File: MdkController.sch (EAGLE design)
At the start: 25 parts, among them M1 SILENTSTEPSTICK, M2 SILENTSTEPSTICK, M3 SILENTSTEPSTICK, M4 SILENTSTEPSTICK, M5 NRF8001-BREAKOUT, U1 ACPL-227, X1 1501_04, X2 1501_04, X3 1501_04

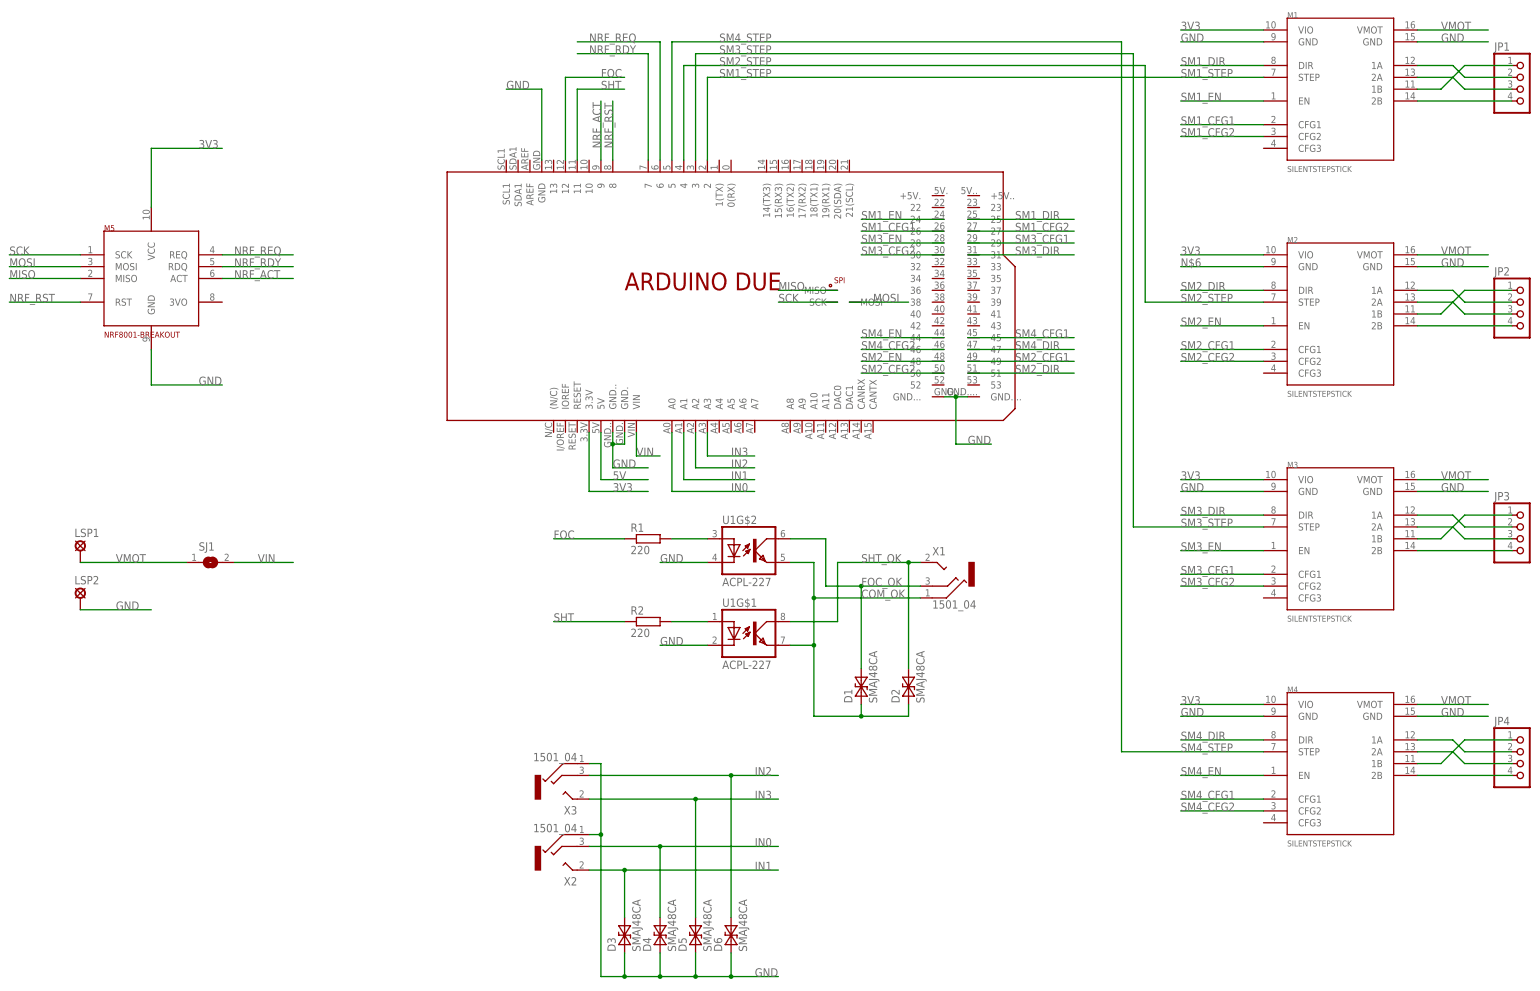
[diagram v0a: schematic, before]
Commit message: Überarbeitung (4. Stepper entfernt, etwas aufgeräumt)
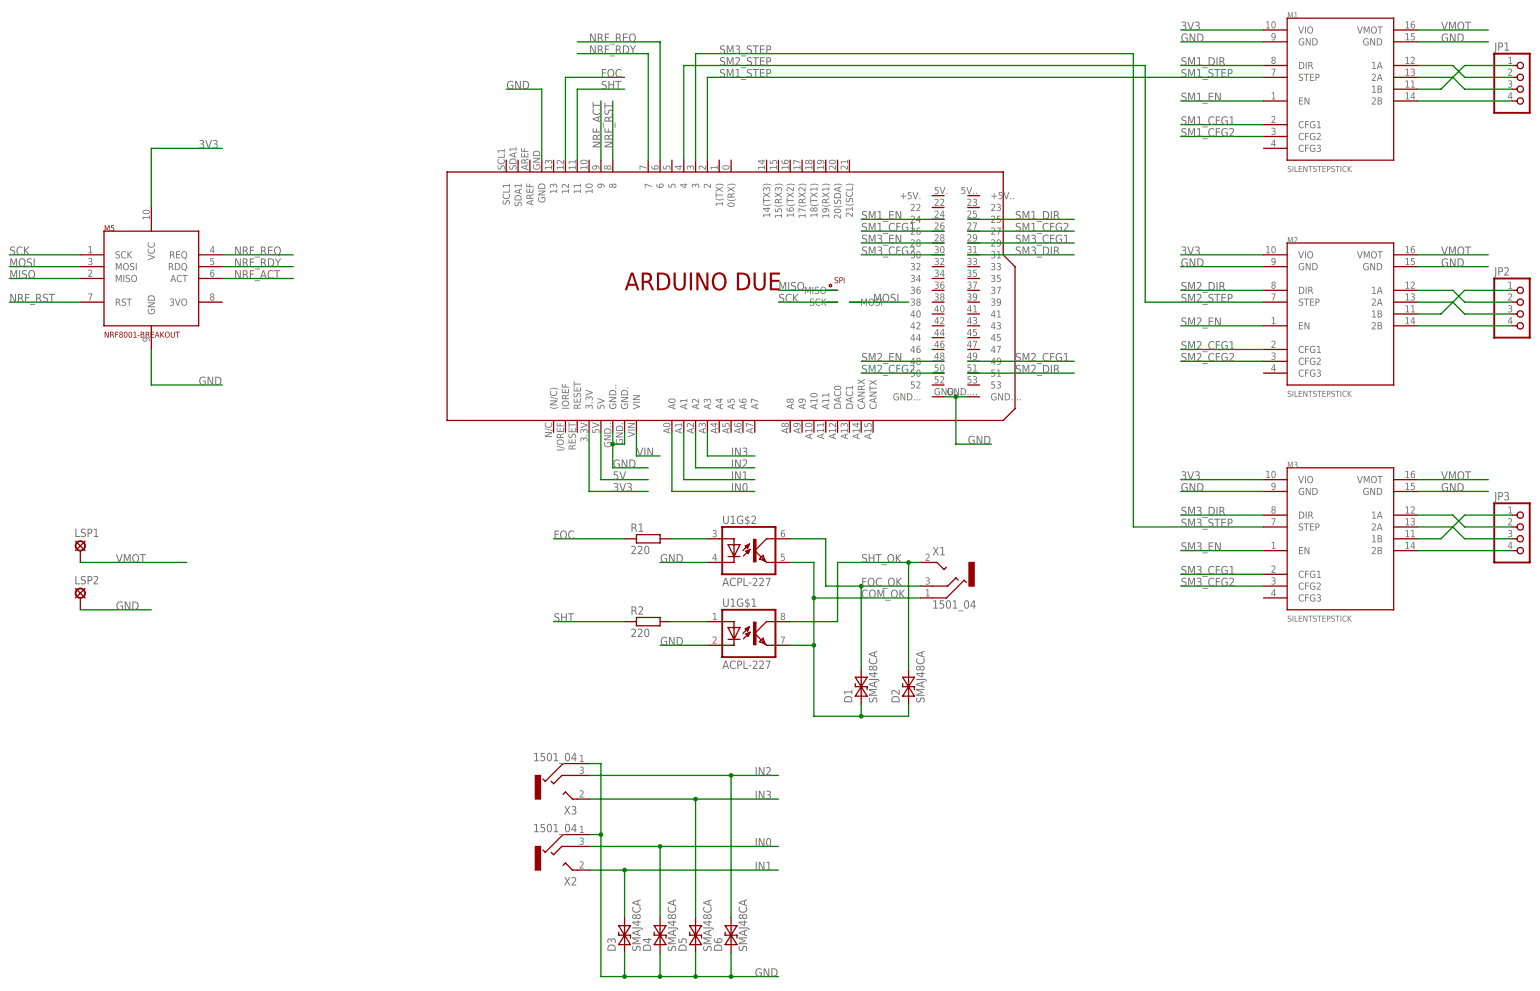
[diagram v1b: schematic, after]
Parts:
- removed JP4: (no value), pinhead:PINHD-1X4
- removed M4: SILENTSTEPSTICK, watterott:SILENTSTEPSTICK
- removed SJ1: (no value), jumper:SJ
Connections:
- removed net N$20: JP4.1, M4.1B
- removed net N$21: JP4.2, M4.1A
- removed net N$22: JP4.3, M4.2A
- removed net N$23: JP4.4, M4.2B
- removed net N$6: M2.GND@1
- removed net SM4_CFG1: M4.CFG1, U$1.45
- removed net SM4_CFG2: M4.CFG2, U$1.46
- removed net SM4_DIR: M4.DIR, U$1.47
- removed net SM4_EN: M4.EN, U$1.44
- removed net SM4_STEP: M4.STEP, U$1.5
- net 3V3: no longer M4.VIO
- net GND: now also M2.GND@1; no longer M4.GND@1, M4.GND@2
- net VIN: no longer SJ1.2
- net VMOT: no longer M4.VMOT, SJ1.1
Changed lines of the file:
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@@
 <?xml version="1.0" encoding="utf-8"?>
 <!DOCTYPE eagle SYSTEM "eagle.dtd">
-<eagle version="7.2.0">
+<eagle version="7.3.0">
 <drawing>
 <settings>
@@
 <part name="M2" library="watterott" deviceset="SILENTSTEPSTICK" device=""/>
 <part name="M3" library="watterott" deviceset="SILENTSTEPSTICK" device=""/>
-<part name="M4" library="watterott" deviceset="SILENTSTEPSTICK" device=""/>
 <part name="R1" library="rcl" deviceset="R-EU_" device="R0805" value="220"/>
 <part name="R2" library="rcl" deviceset="R-EU_" device="R0805" value="220"/>
@@
 <part name="JP2" library="pinhead" deviceset="PINHD-1X4" device=""/>
 <part name="JP3" library="pinhead" deviceset="PINHD-1X4" device=""/>
-<part name="JP4" library="pinhead" deviceset="PINHD-1X4" device=""/>
 <part name="LSP1" library="solpad" deviceset="SE14" device=""/>
 <part name="LSP2" library="solpad" deviceset="SE14" device=""/>
-<part name="SJ1" library="jumper" deviceset="SJ" device=""/>
 </parts>
 <sheets>
@@
 <instance part="M2" gate="G$1" x="215.9" y="134.62"/>
 <instance part="M3" gate="G$1" x="215.9" y="86.36"/>
-<instance part="M4" gate="G$1" x="215.9" y="38.1"/>
 <instance part="R1" gate="G$1" x="78.74" y="114.3"/>
 <instance part="R2" gate="G$1" x="78.74" y="96.52"/>
@@
 <instance part="JP2" gate="A" x="266.7" y="162.56"/>
 <instance part="JP3" gate="A" x="266.7" y="114.3"/>
-<instance part="JP4" gate="A" x="266.7" y="66.04"/>
 <instance part="LSP1" gate="1" x="-43.18" y="111.76"/>
 <instance part="LSP2" gate="1" x="-43.18" y="101.6"/>
-<instance part="SJ1" gate="1" x="-15.24" y="109.22"/>
 </instances>
 <busses>
@@
 </segment>
 </net>
-<net name="SM4_EN" class="0">
-<segment>
-<wire x1="142.24" y1="157.48" x2="124.46" y2="157.48" width="0.1524" layer="91"/>
-<pinref part="U$1" gate="G$1" pin="44"/>
-<label x="124.46" y="157.48" size="1.778" layer="95"/>
-</segment>
-<segment>
-<pinref part="M4" gate="G$1" pin="EN"/>
-<wire x1="210.82" y1="63.5" x2="193.04" y2="63.5" width="0.1524" layer="91"/>
-<label x="193.04" y="63.5" size="1.778" layer="95"/>
-</segment>
-</net>
-<net name="SM4_CFG1" class="0">
-<segment>
-<wire x1="147.32" y1="157.48" x2="170.18" y2="157.48" width="0.1524" layer="91"/>
-<pinref part="U$1" gate="G$1" pin="45"/>
-<label x="157.48" y="157.48" size="1.778" layer="95"/>
-</segment>
-<segment>
-<pinref part="M4" gate="G$1" pin="CFG1"/>
-<wire x1="210.82" y1="58.42" x2="193.04" y2="58.42" width="0.1524" layer="91"/>
-<label x="193.04" y="58.42" size="1.778" layer="95"/>
-</segment>
-</net>
 <net name="SM3_CFG2" class="0">
 <segment>
@@
 <wire x1="210.82" y1="104.14" x2="193.04" y2="104.14" width="0.1524" layer="91"/>
 <label x="193.04" y="104.14" size="1.778" layer="95"/>
-</segment>
-</net>
-<net name="SM4_DIR" class="0">
-<segment>
-<wire x1="147.32" y1="154.94" x2="170.18" y2="154.94" width="0.1524" layer="91"/>
-<pinref part="U$1" gate="G$1" pin="47"/>
-<label x="157.48" y="154.94" size="1.778" layer="95"/>
-</segment>
-<segment>
-<pinref part="M4" gate="G$1" pin="DIR"/>
-<wire x1="210.82" y1="71.12" x2="193.04" y2="71.12" width="0.1524" layer="91"/>
-<label x="193.04" y="71.12" size="1.778" layer="95"/>
-</segment>
-</net>
-<net name="SM4_CFG2" class="0">
-<segment>
-<wire x1="142.24" y1="154.94" x2="124.46" y2="154.94" width="0.1524" layer="91"/>
-<pinref part="U$1" gate="G$1" pin="46"/>
-<label x="124.46" y="154.94" size="1.778" layer="95"/>
-</segment>
-<segment>
-<pinref part="M4" gate="G$1" pin="CFG2"/>
-<wire x1="210.82" y1="55.88" x2="193.04" y2="55.88" width="0.1524" layer="91"/>
-<label x="193.04" y="55.88" size="1.778" layer="95"/>
 </segment>
 </net>
@@
 </segment>
 </net>
-<net name="SM4_STEP" class="0">
-<segment>
-<pinref part="U$1" gate="G$1" pin="5"/>
-<wire x1="83.82" y1="195.58" x2="83.82" y2="220.98" width="0.1524" layer="91"/>
-<wire x1="83.82" y1="220.98" x2="180.34" y2="220.98" width="0.1524" layer="91"/>
-<pinref part="M4" gate="G$1" pin="STEP"/>
-<wire x1="180.34" y1="220.98" x2="180.34" y2="68.58" width="0.1524" layer="91"/>
-<wire x1="180.34" y1="68.58" x2="210.82" y2="68.58" width="0.1524" layer="91"/>
-<label x="93.98" y="220.98" size="1.778" layer="95"/>
-<label x="193.04" y="68.58" size="1.778" layer="95"/>
-</segment>
-</net>
 <net name="3V3" class="1">
 <segment>
@@
 <wire x1="66.04" y1="124.46" x2="78.74" y2="124.46" width="0.1524" layer="91"/>
 <label x="71.12" y="124.46" size="1.778" layer="95"/>
-</segment>
-<segment>
-<pinref part="M4" gate="G$1" pin="VIO"/>
-<wire x1="210.82" y1="78.74" x2="193.04" y2="78.74" width="0.1524" layer="91"/>
-<label x="193.04" y="78.74" size="1.778" layer="95"/>
 </segment>
 <segment>
@@
 </segment>
 <segment>
-<pinref part="M4" gate="G$1" pin="GND@2"/>
-<wire x1="243.84" y1="76.2" x2="259.08" y2="76.2" width="0.1524" layer="91"/>
-<label x="248.92" y="76.2" size="1.778" layer="95"/>
-</segment>
-<segment>
-<pinref part="M4" gate="G$1" pin="GND@1"/>
-<wire x1="210.82" y1="76.2" x2="193.04" y2="76.2" width="0.1524" layer="91"/>
-<label x="193.04" y="76.2" size="1.778" layer="95"/>
-</segment>
-<segment>
 <pinref part="M3" gate="G$1" pin="GND@1"/>
 <wire x1="210.82" y1="124.46" x2="193.04" y2="124.46" width="0.1524" layer="91"/>
@@
 <wire x1="-43.18" y1="99.06" x2="-27.94" y2="99.06" width="0.1524" layer="91"/>
 <label x="-35.56" y="99.06" size="1.778" layer="95"/>
+</segment>
+<segment>
+<pinref part="M2" gate="G$1" pin="GND@1"/>
+<wire x1="210.82" y1="172.72" x2="193.04" y2="172.72" width="0.1524" layer="91"/>
+<label x="193.04" y="172.72" size="1.778" layer="95"/>
 </segment>
 </net>
@@
 </segment>
 </net>
-<net name="N$6" class="0">
-<segment>
-<pinref part="M2" gate="G$1" pin="GND@1"/>
-<wire x1="210.82" y1="172.72" x2="193.04" y2="172.72" width="0.1524" layer="91"/>
-<label x="193.04" y="172.72" size="1.778" layer="95"/>
-</segment>
-</net>
 <net name="N$3" class="2">
 <segment>
@@
 </segment>
 </net>
-<net name="N$20" class="2">
-<segment>
-<pinref part="M4" gate="G$1" pin="1B"/>
-<wire x1="243.84" y1="66.04" x2="248.92" y2="66.04" width="0.1524" layer="91"/>
-<wire x1="248.92" y1="66.04" x2="254" y2="71.12" width="0.1524" layer="91"/>
-<pinref part="JP4" gate="A" pin="1"/>
-<wire x1="254" y1="71.12" x2="264.16" y2="71.12" width="0.1524" layer="91"/>
-</segment>
-</net>
-<net name="N$21" class="2">
-<segment>
-<pinref part="M4" gate="G$1" pin="1A"/>
-<wire x1="243.84" y1="71.12" x2="251.46" y2="71.12" width="0.1524" layer="91"/>
-<wire x1="251.46" y1="71.12" x2="254" y2="68.58" width="0.1524" layer="91"/>
-<pinref part="JP4" gate="A" pin="2"/>
-<wire x1="254" y1="68.58" x2="264.16" y2="68.58" width="0.1524" layer="91"/>
-</segment>
-</net>
-<net name="N$22" class="2">
-<segment>
-<pinref part="M4" gate="G$1" pin="2A"/>
-<wire x1="243.84" y1="68.58" x2="251.46" y2="68.58" width="0.1524" layer="91"/>
-<wire x1="251.46" y1="68.58" x2="254" y2="66.04" width="0.1524" layer="91"/>
-<pinref part="JP4" gate="A" pin="3"/>
-<wire x1="254" y1="66.04" x2="264.16" y2="66.04" width="0.1524" layer="91"/>
-</segment>
-</net>
-<net name="N$23" class="2">
-<segment>
-<pinref part="M4" gate="G$1" pin="2B"/>
-<pinref part="JP4" gate="A" pin="4"/>
-<wire x1="243.84" y1="63.5" x2="264.16" y2="63.5" width="0.1524" layer="91"/>
-</segment>
-</net>
 <net name="VMOT" class="2">
 <segment>
@@
 <wire x1="-43.18" y1="109.22" x2="-20.32" y2="109.22" width="0.1524" layer="91"/>
 <label x="-35.56" y="109.22" size="1.778" layer="95"/>
-<pinref part="SJ1" gate="1" pin="1"/>
-</segment>
-<segment>
-<pinref part="M4" gate="G$1" pin="VMOT"/>
-<wire x1="243.84" y1="78.74" x2="259.08" y2="78.74" width="0.1524" layer="91"/>
-<label x="248.92" y="78.74" size="1.778" layer="95"/>
 </segment>
 <segment>
@@
 <net name="VIN" class="1">
 <segment>
-<wire x1="-10.16" y1="109.22" x2="2.54" y2="109.22" width="0.1524" layer="91"/>
-<label x="-5.08" y="109.22" size="1.778" layer="95"/>
-<pinref part="SJ1" gate="1" pin="2"/>
-</segment>
-<segment>
 <pinref part="U$1" gate="G$1" pin="VIN"/>
